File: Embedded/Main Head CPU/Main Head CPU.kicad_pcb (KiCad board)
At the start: 4 copper layers, 50 x 47.5 mm, 49 parts, among them J1 10171746-00021LF, J10 Fan 1, J11 Substructure Power, J12 Head Power, J13 MicroSD, J14 Mic, J15 I2C, J2 Maw, J3 Tongue, J4 Left Fin, J5 Right Fin, J6 Scales, J7 Extra, J8 Buttons, J9 Fan 0, Q1 DMG3402L, Q2 DMG3402L, SW1 Boot, SW2 RST, U1 Sensored, U3 LD1117S33TR_SOT223, U4 LD1117S50TR_SOT223, U5 Substructure

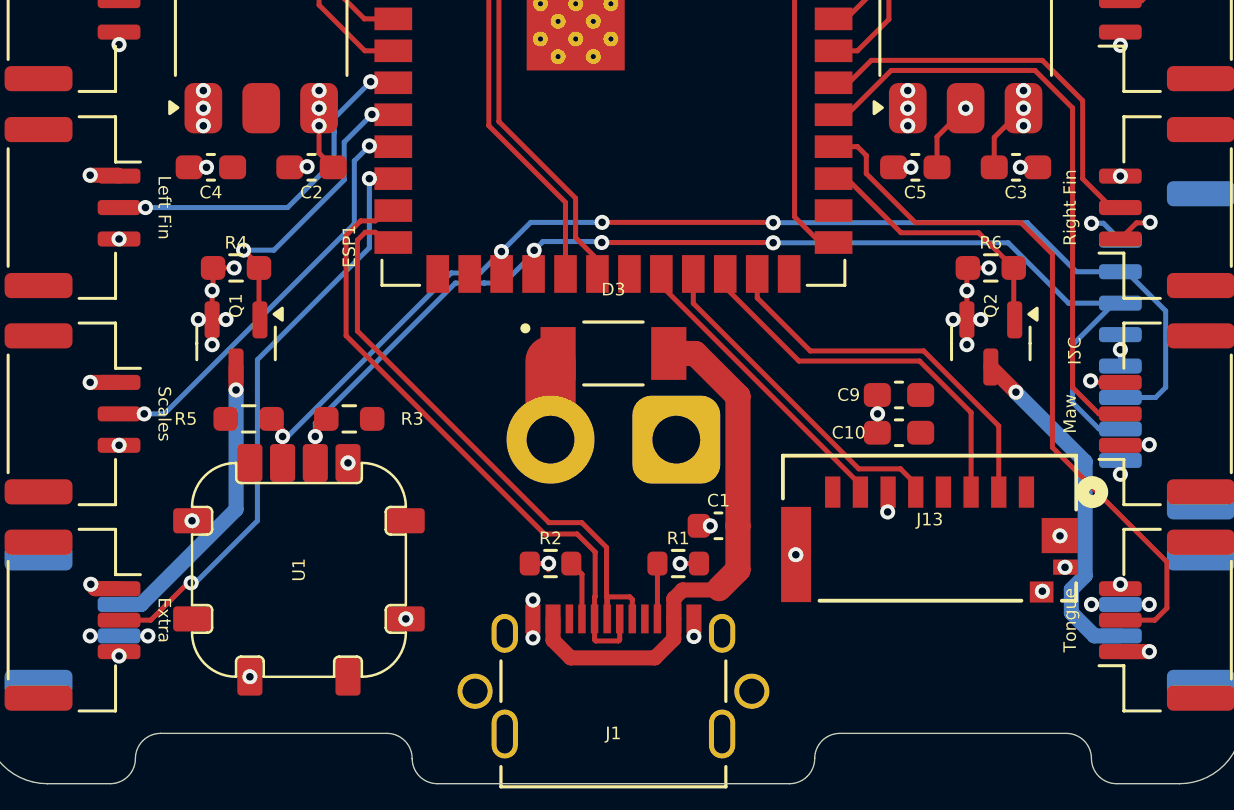
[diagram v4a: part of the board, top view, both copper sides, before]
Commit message: Modified Addressable LED strip labels for general systems
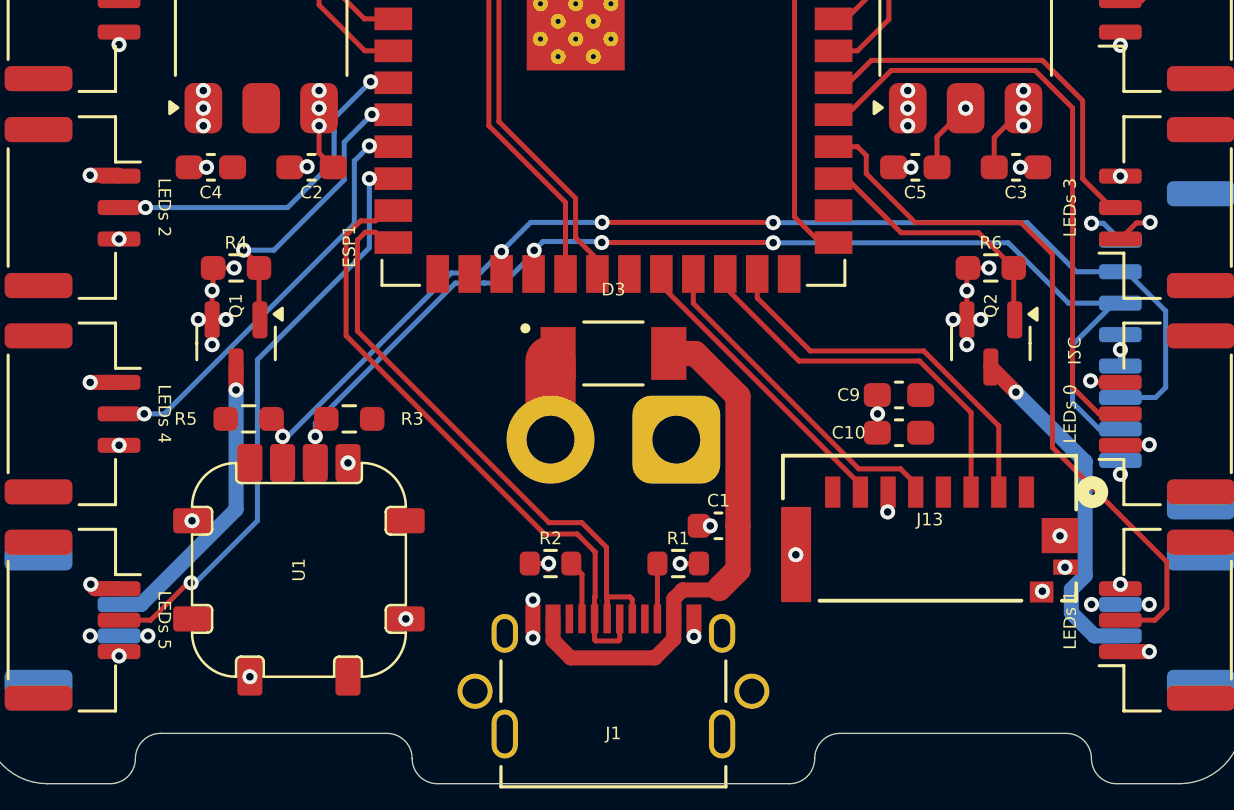
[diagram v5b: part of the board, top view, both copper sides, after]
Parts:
- J2: value Maw -> LEDs 0
- J3: value Tongue -> LEDs 1
- J4: value Left Fin -> LEDs 2
- J5: value Right Fin -> LEDs 3
- J6: value Scales -> LEDs 4
- J7: value Extra -> LEDs 5
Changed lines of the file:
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@@
 			)
 		)
-		(property "Value" "Right Fin"
+		(property "Value" "LEDs 3"
 			(at 0 -3.85 90)
 			(layer "F.SilkS")
@@
 			)
 		)
-		(property "Value" "Extra"
+		(property "Value" "LEDs 5"
 			(at 0 -3.65 270)
 			(unlocked yes)
@@
 			)
 		)
-		(property "Value" "Left Fin"
+		(property "Value" "LEDs 2"
 			(at 0 -3.65 270)
 			(unlocked yes)
@@
 			)
 		)
-		(property "Value" "Scales"
+		(property "Value" "LEDs 4"
 			(at 0 -3.65 270)
 			(unlocked yes)
@@
 			)
 		)
-		(property "Value" "Tongue"
+		(property "Value" "LEDs 1"
 			(at 0 -3.85 90)
 			(layer "F.SilkS")
@@
 			)
 		)
-		(property "Value" "Maw"
+		(property "Value" "LEDs 0"
 			(at 0 -3.85 90)
 			(layer "F.SilkS")

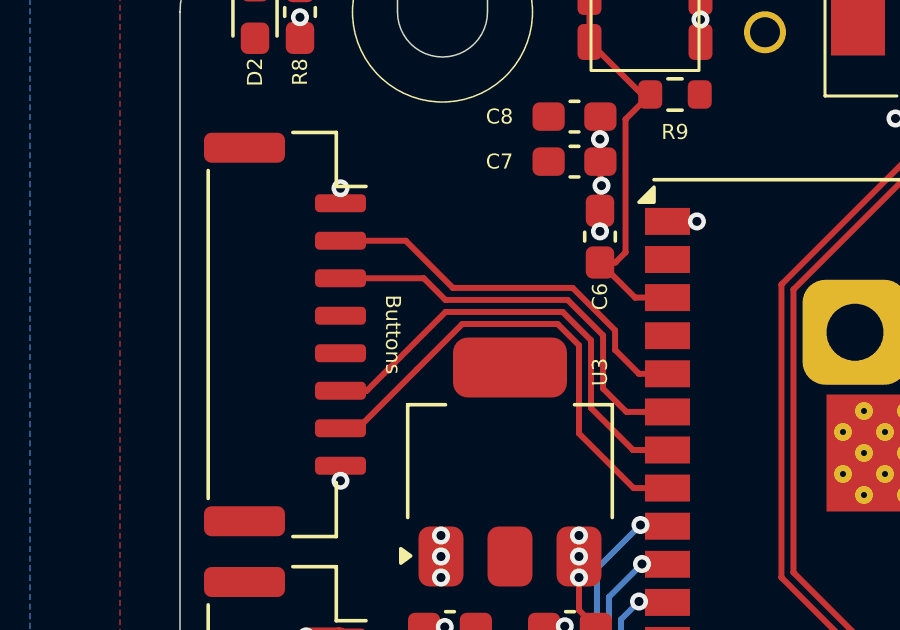
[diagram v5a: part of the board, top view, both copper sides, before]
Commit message: Added Pull down resistors to buttons
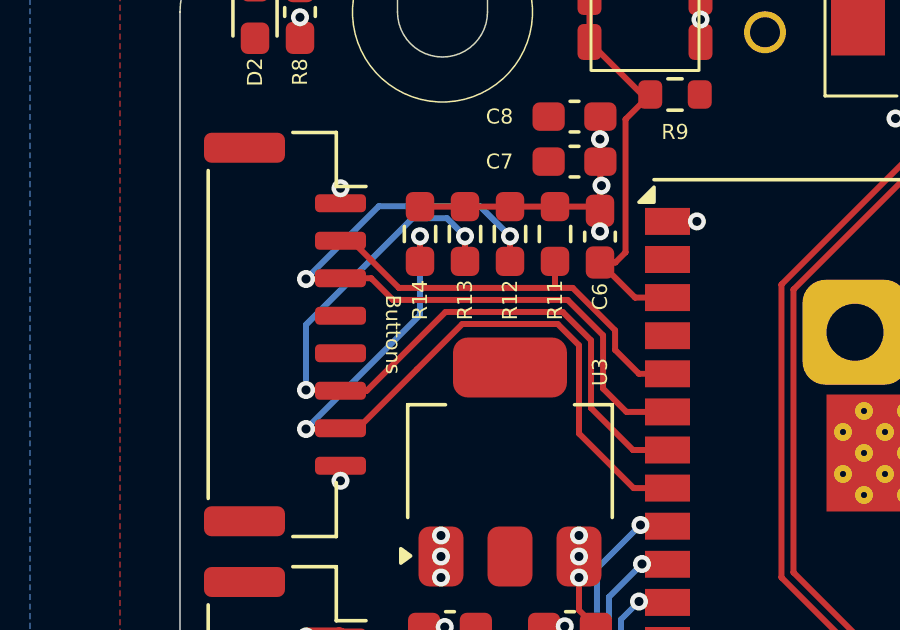
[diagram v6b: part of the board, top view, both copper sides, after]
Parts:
- added R11: 10K, Resistor_SMD:R_0603_1608Metric_Pad0.98x0.95mm_HandSolder, F.Cu at (87.5, 52.4)
- added R12: 10K, Resistor_SMD:R_0603_1608Metric_Pad0.98x0.95mm_HandSolder, F.Cu at (86.0, 52.4)
- added R13: 10K, Resistor_SMD:R_0603_1608Metric_Pad0.98x0.95mm_HandSolder, F.Cu at (84.5, 52.4)
- added R14: 10K, Resistor_SMD:R_0603_1608Metric_Pad0.98x0.95mm_HandSolder, F.Cu at (83.0, 52.4)
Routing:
- net Button 2: track 15.2 -> 26.4 mm, vias 0 -> 2
- net Button 1: track 13.8 -> 24.0 mm, vias 0 -> 2
- net Button 3: track 16.4 -> 26.4 mm, vias 0 -> 2
- net GND: track 37.6 -> 43.6 mm
- net Button 0: track 13.1 -> 14.0 mm

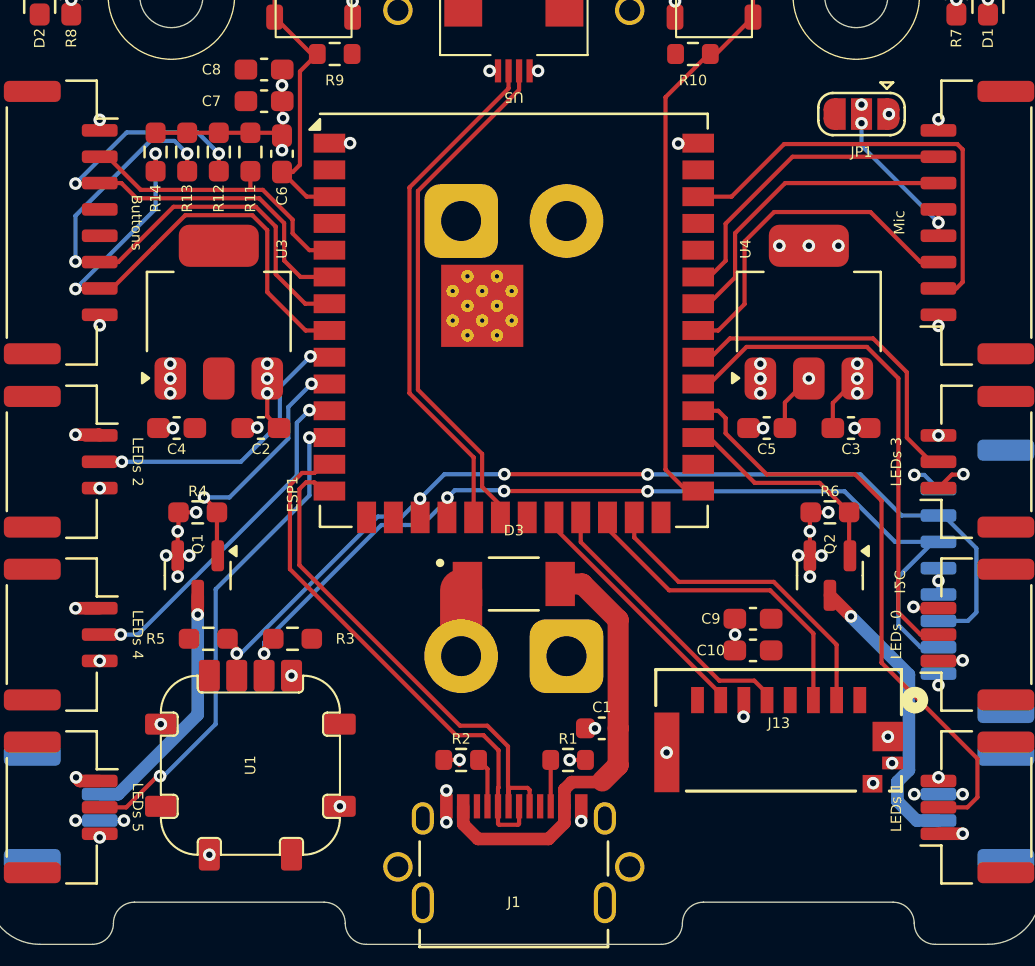
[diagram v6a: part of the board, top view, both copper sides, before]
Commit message: Modified Addressable LED ports for general (instead of static config names)
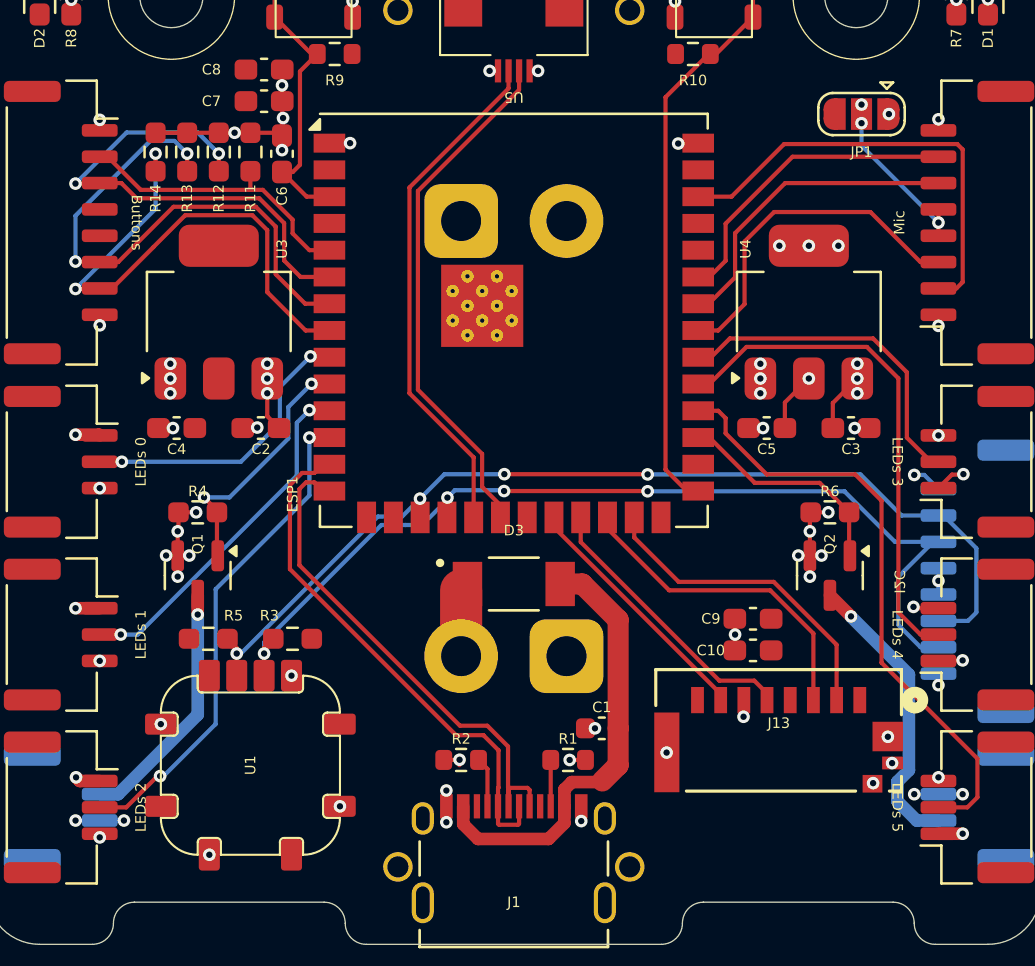
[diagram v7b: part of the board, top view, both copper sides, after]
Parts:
- moved J2 44.3 mm to (78.5, 67.1), turned to -90 degrees
- moved J3 44.3 mm to (78.5, 75.3), turned to -90 degrees
- moved J6 43.5 mm to (122.0, 75.3), turned to 90 degrees
- moved J7 43.5 mm to (122.0, 83.5), turned to 90 degrees
- moved J4 16.4 mm to (78.5, 83.5)
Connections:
- ESP1 pad 11: Addr LED 4 -> Addr LED 1
- ESP1 pad 12: Addr LED 5 -> Addr LED 2
- ESP1 pad 30: Addr LED 1 -> Addr LED 5
- ESP1 pad 31: Addr LED 0 -> Addr LED 4
- ESP1 pad 9: Addr LED 2 -> Addr LED 0
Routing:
- net Addr LED 1: track 28.9 -> 16.8 mm, vias 0 -> 2
- net Addr LED 0: track 24.3 -> 14.0 mm, vias 0 -> 2
- net Addr LED 2: track 14.0 -> 23.5 mm
- net Addr LED 4: track 16.8 -> 24.3 mm, vias 2 -> 0
- net Addr LED 5: track 23.5 -> 28.9 mm, vias 2 -> 0
- net GND: track 43.6 -> 44.4 mm, vias 59 -> 60

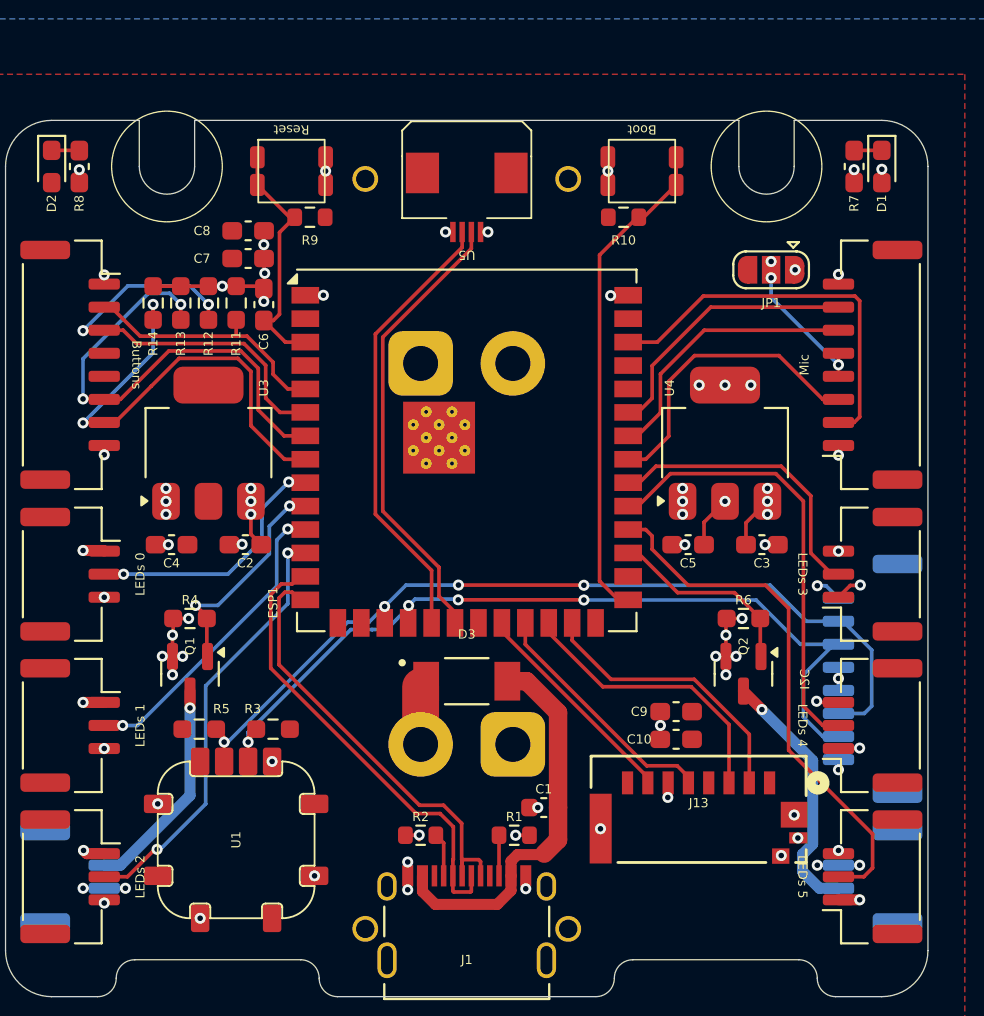
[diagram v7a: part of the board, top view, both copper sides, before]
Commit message: Added UART Pins to Expansion
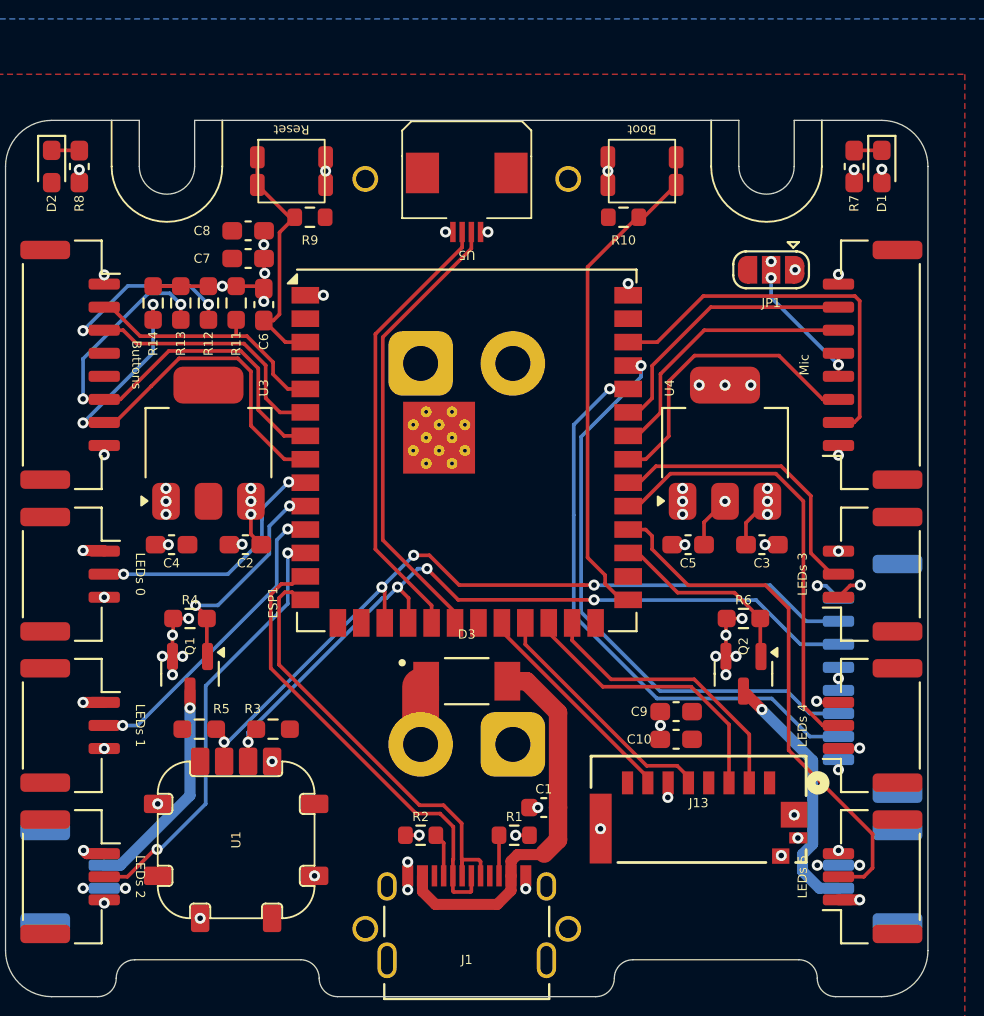
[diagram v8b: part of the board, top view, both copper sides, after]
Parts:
- J15: value I2C -> Expansion
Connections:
- ESP1 pad 36: unconnected-(ESP1-U0RXD/GPIO44/CLK_OUT2-Pad36) -> Expansion RXD
- ESP1 pad 37: unconnected-(ESP1-U0TXD/GPIO43/CLK_OUT1-Pad37) -> Expansion TXD
- J15 pad 4: +3V3 -> +5V
- J15 pad 5: +3V3 -> +5V
- J15 pad 6: I2C SDA -> Expansion TXD
- J15 pad 7: I2C SCL -> Expansion RXD
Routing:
- net Expansion TXD: track 0.00 -> 31.6 mm, vias 0 -> 1
- net Expansion RXD: track 0.00 -> 31.2 mm, vias 0 -> 1
- net I2C SDA: track 47.9 -> 43.2 mm
- net I2C SCL: track 46.7 -> 42.3 mm
- net +5V: track 136.7 -> 139.1 mm, vias 16 -> 17
- net +3V3: track 1.25 -> 0.00 mm, vias 1 -> 0
